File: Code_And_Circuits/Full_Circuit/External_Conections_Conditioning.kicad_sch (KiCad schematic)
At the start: 31 parts, among them J2 Main_Power_In_JST-XH, J3 Warning_Lights_JST-XH, J4 Signals_RPM_Temp_Fuel_JST-XH, J5 Speed_Pulser_Setup_Signal_JST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, U1 R-78E3.3-0.5, U3 TEC2-1219WI, U4 L7805

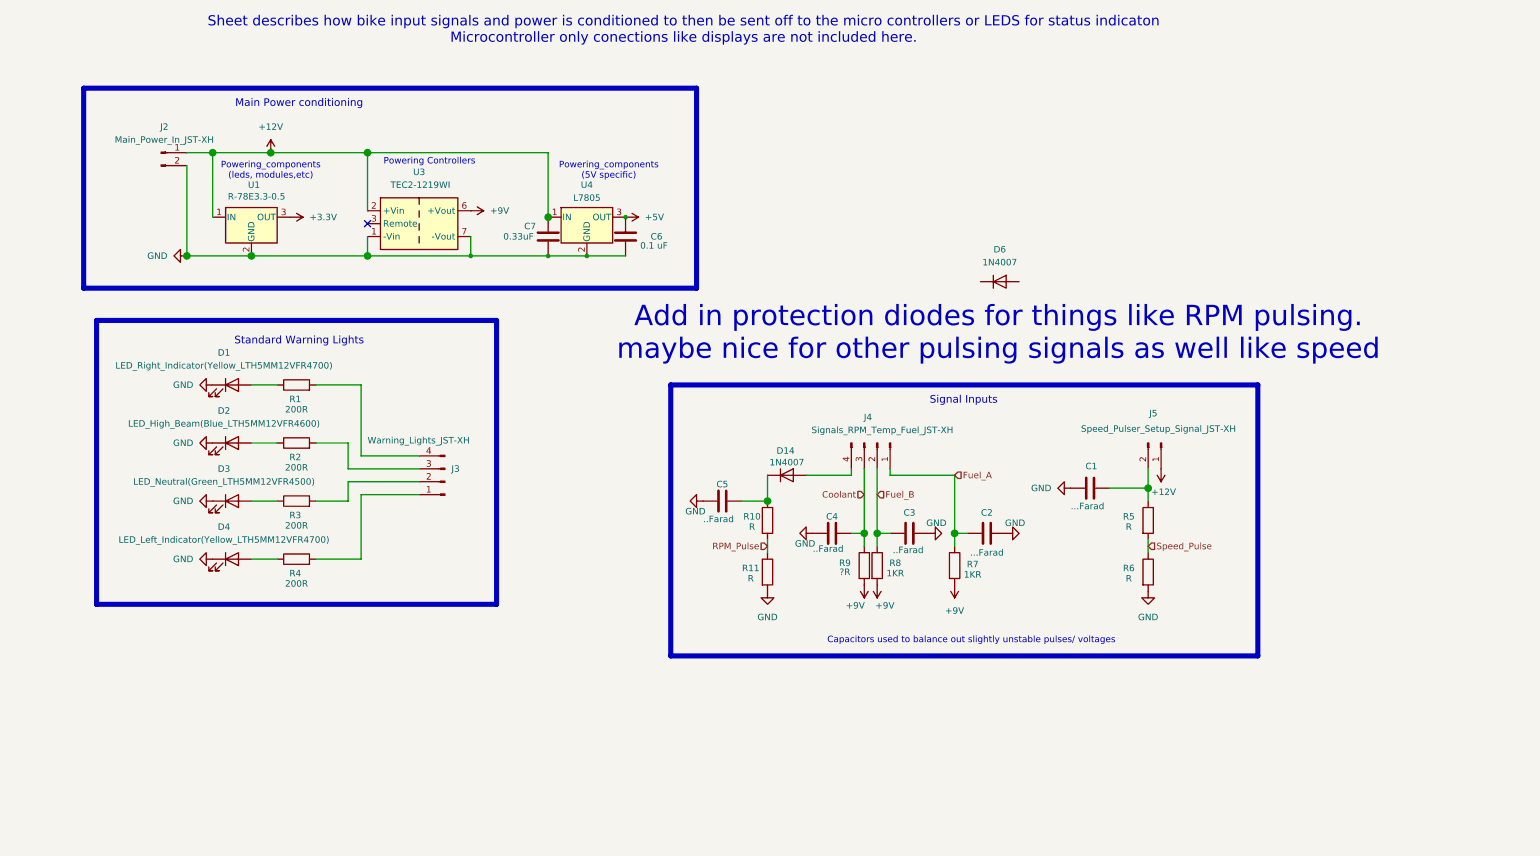
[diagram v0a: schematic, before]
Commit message: Finished schematic need to do PCB design and get Tachometer reference
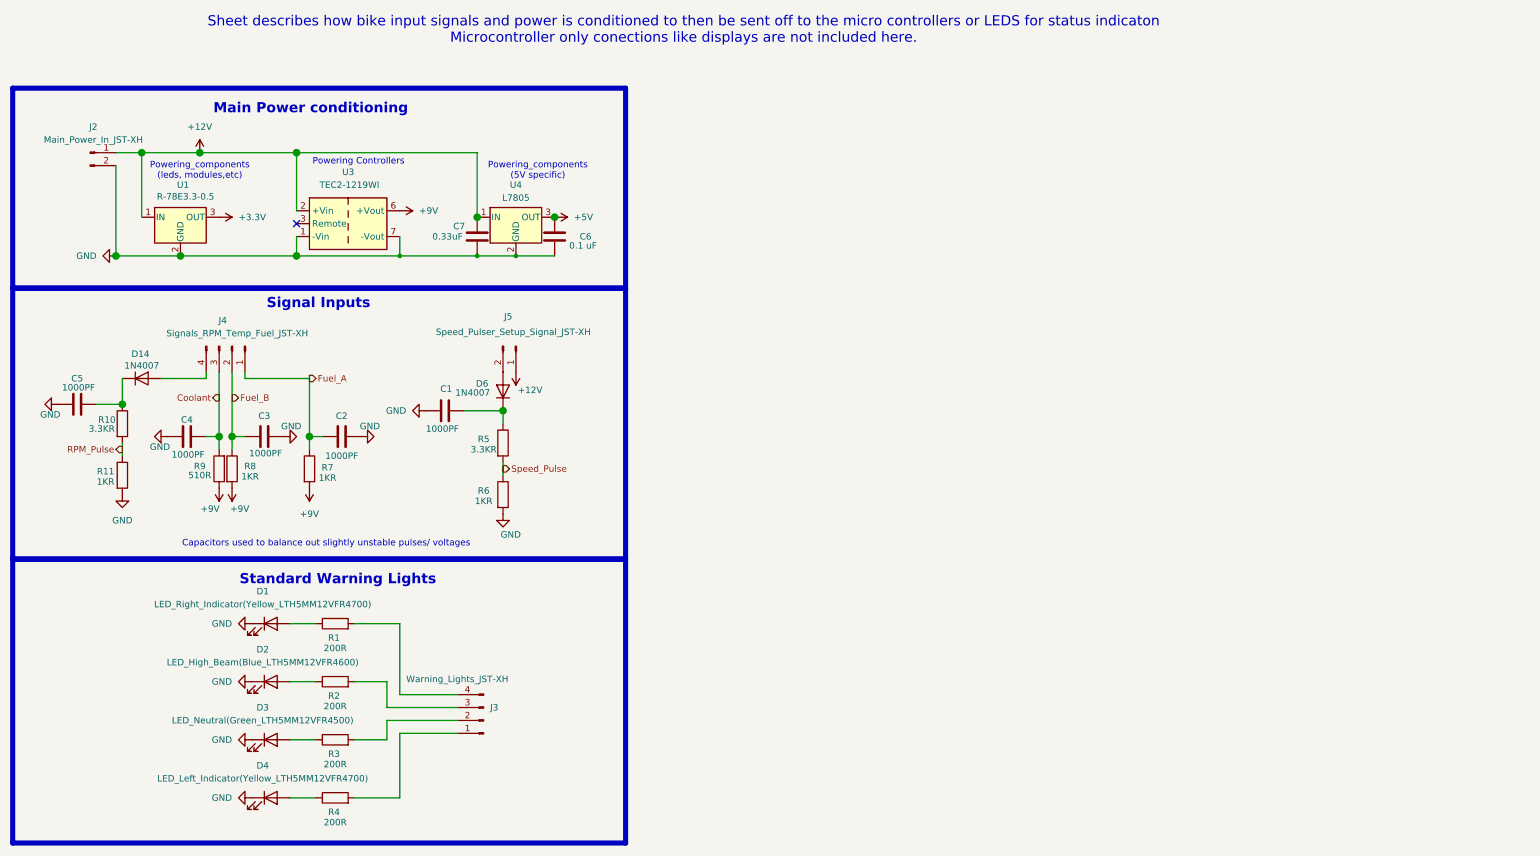
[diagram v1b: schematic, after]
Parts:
- C1, C2: value ...Farad -> 1000PF
- C3, C4, C5: value ..Farad -> 1000PF
- R10, R5: value R -> 3.3KR
- R11, R6: value R -> 1KR
- R9: value ?R -> 510R
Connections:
- net at C1.1, R5.1: now also D6.1 (K); no longer J5.2 (Pin_2)
- net at D6.2 (A): now also J5.2 (Pin_2)
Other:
- note removed: "Add in protection diodes for things like RPM pulsing. maybe nice for other pulsing signals as well like speed"
- moved on the sheet: C1, C2, C3, C4, C5, C6, C7, D1, D14, D2, D3, D4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

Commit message: Reconfired some pin assignments for cleaner layout and adding reference footprints and mostly layed out board, due to space limits logging section has been ommitted
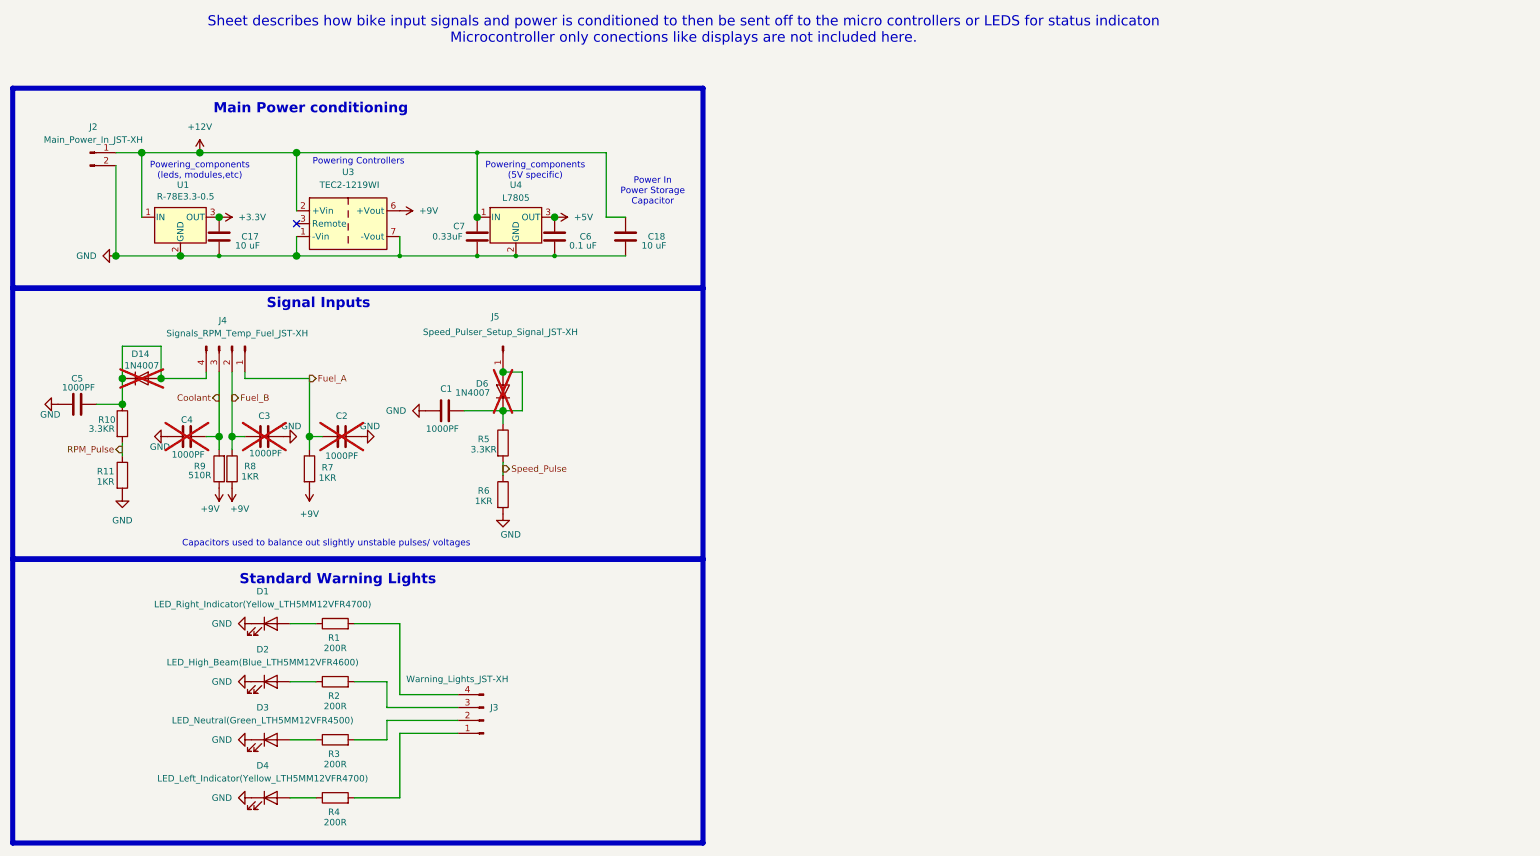
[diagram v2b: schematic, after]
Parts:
- added C17, C18: 10 uF, Capacitor_THT:C_Disc_D3.0mm_W1.6mm_P2.50mm, symbol Device:C
- C1, C5, C6, C7: footprint Capacitor_THT:C_Disc_D3.0mm_W2.0mm_P2.50mm -> Capacitor_SMD:C_0805_2012Metric_Pad1.18x1.45mm_HandSolder
- C2, C3, C4, D14, D6: now not fitted
- J5: footprint Connector_JST:JST_XH_B2B-XH-A_1x02_P2.50mm_Vertical -> Connector_Wire:SolderWirePad_1x01_SMD_1x2mm; symbol Connector:Conn_01x02_Pin -> Connector:Conn_01x01_Pin
- R1, R10, R11, R2, R3, R4, R5, R6, R7, R8, R9: footprint Resistor_THT:R_Axial_DIN0204_L3.6mm_D1.6mm_P7.62mm_Horizontal -> Resistor_SMD:R_0805_2012Metric_Pad1.20x1.40mm_HandSolder
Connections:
- net +12V: now also C18.1; no longer J5.1 (Pin_1)
- net +3.3V: now also C17.1
- net GND: now also C17.2, C18.2
- net at C1.1, D6.1 (K), R5.1: now also D6.2 (A), J5.1 (Pin_1)
- net at C5.2, D14.1 (K), R10.1: now also D14.2 (A), J4.4 (Pin_4)
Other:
- note added: "Power In Power Storage Capacitor"
